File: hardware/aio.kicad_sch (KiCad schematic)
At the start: 39 parts, among them IC1 DAC7562SDGSR, J10 TB007-508-02BE, J11 TB007-508-02BE, J12 TB007-508-02BE, J9 TB007-508-02BE, Q4 MMBT2907ALT1G, Q5 BSP171PH6327XTSA1, U13 TLV9301IDBVR, U14 TLV9301IDBVR, U15 XTR111AIDGQR

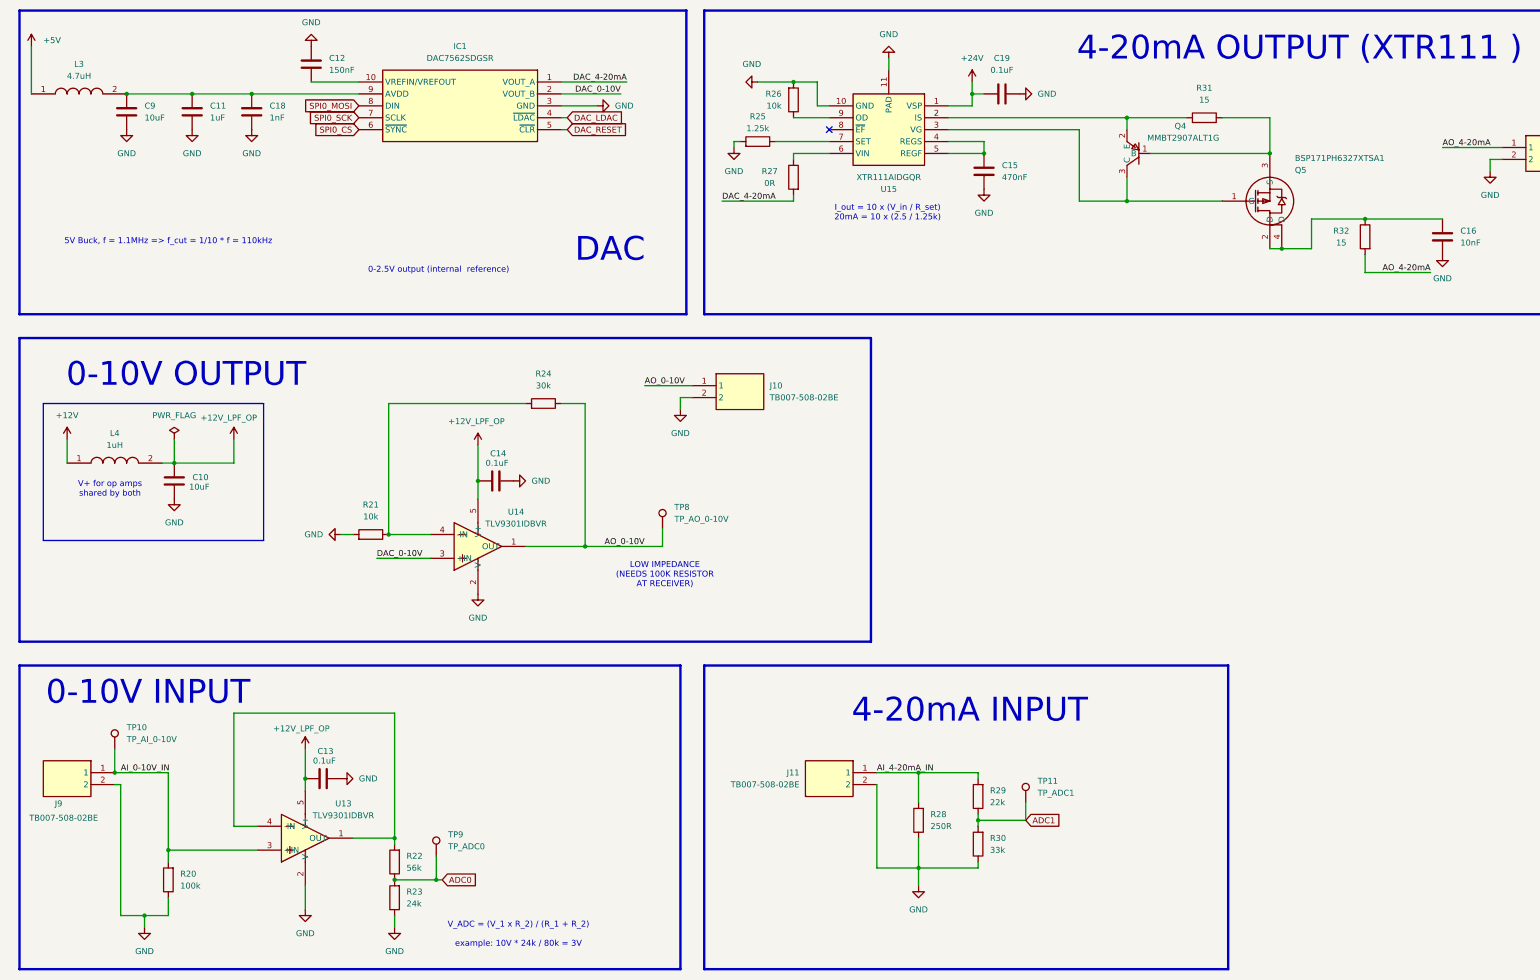
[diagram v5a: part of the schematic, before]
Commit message: Modbus, small schematic changes
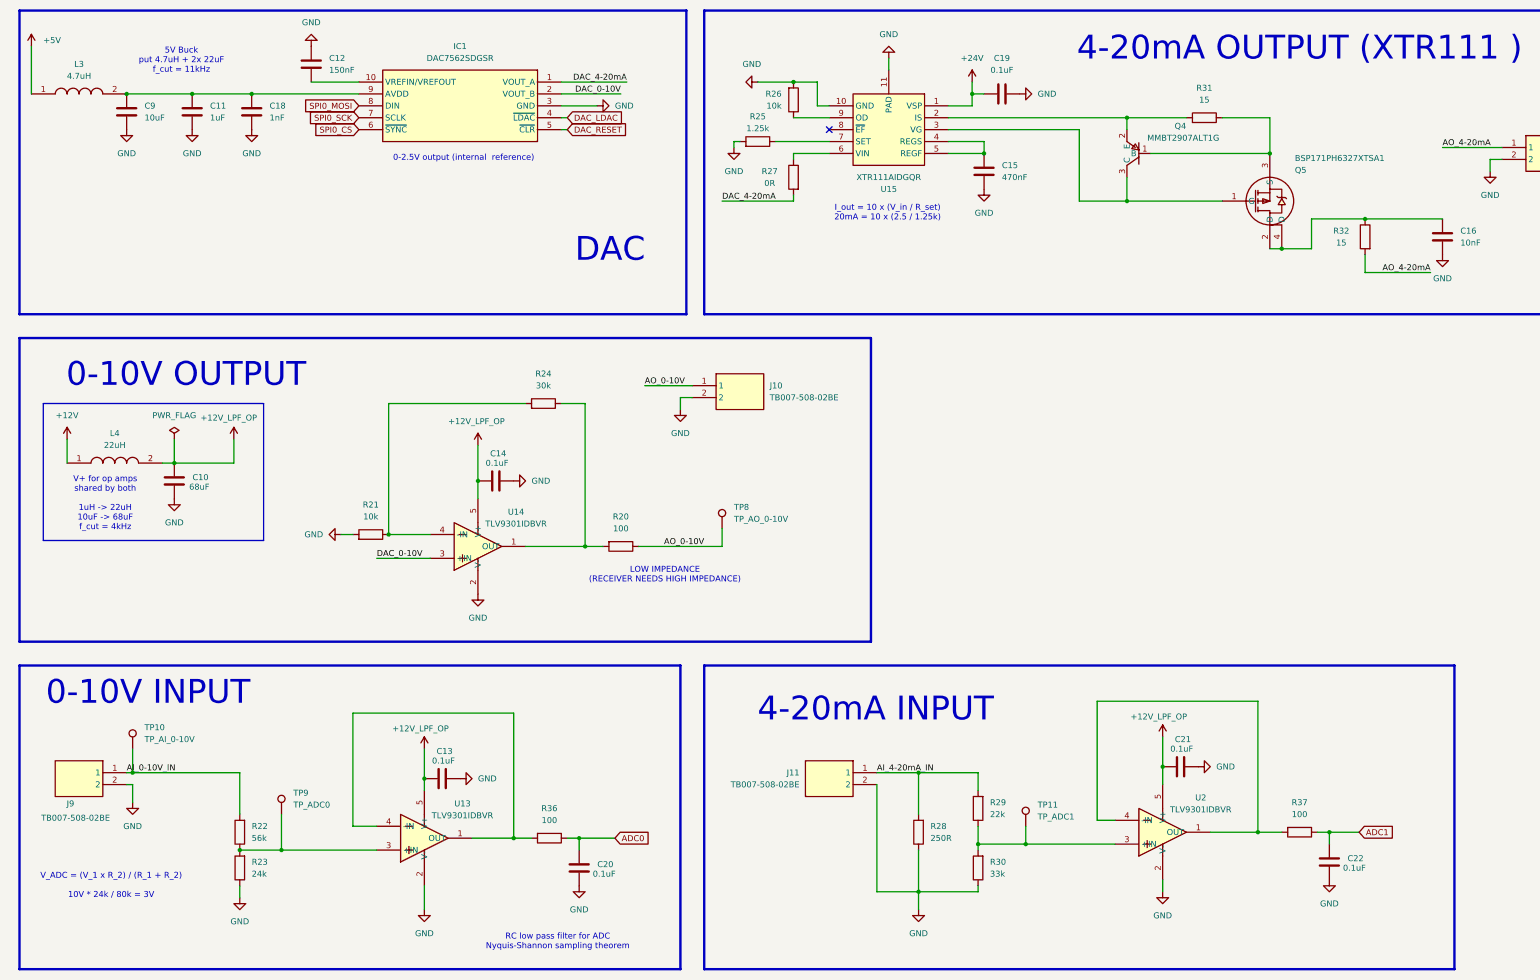
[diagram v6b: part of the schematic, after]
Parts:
- added C20, C21, C22: 0.1uF, Capacitor_SMD:C_1206_3216Metric_Pad1.33x1.80mm_HandSolder, symbol Device:C
- added R36, R37: 100, Resistor_SMD:R_1206_3216Metric_Pad1.30x1.75mm_HandSolder, symbol Device:R
- added U2: TLV9301IDBVR, EasyEDA:SOT-23-5_L3.0-W1.7-P0.95-LS2.8-BR, symbol EasyEDA:TLV9301IDBVR
- C10: value 10uF -> 68uF
- L4: value 1uH -> 22uH
- R20: value 100k -> 100
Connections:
- net +12V_LPF_OP: now also C21.1, U2.5 (V+)
- net ADC0: now also C20.1, R36.1; no longer R22.1, R23.2, TP9.1
- net ADC1: now also C22.1, R37.1; no longer R29.1, R30.2, TP11.1
- net AI_0-10V_IN: now also R22.2; no longer R20.2, U13.3 (+IN)
- net AO_0-10V: now also R20.1; no longer R24.1, U14.1 (OUT)
- net GND: now also C20.2, C21.2, C22.2, U2.2 (V-); no longer R20.1
- net at U13.1 (OUT), U13.4 (-IN): now also R36.2; no longer R22.2
- new net: R20.2, R24.1, U14.1 (OUT)
- new net: R37.2, U2.1 (OUT), U2.4 (-IN)
- new net: R29.1, R30.2, TP11.1, U2.3 (+IN)
- new net: R22.1, R23.2, TP9.1, U13.3 (+IN)
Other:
- note added: "5V Buck put 4.7uH + 2x 22uF f_cut = 11kHz"
- note added: "LOW IMPEDANCE (RECEIVER NEEDS HIGH IMPEDANCE)"
- note added: "RC low pass filter for ADC Nyquis-Shannon sampling theorem"
- note added: "V+ for op amps shared by both 1uH -> 22uH 10uF -> 68uF f_cut = 4kHz"
- note added: "V_ADC = (V_1 x R_2) / (R_1 + R_2) 10V * 24k / 80k = 3V"
- note removed: "5V Buck, f = 1.1MHz => f_cut = 1/10 * f = 110kHz"
- note removed: "LOW IMPEDANCE (NEEDS 100K RESISTOR AT RECEIVER)"
- note removed: "V+ for op amps shared by both"
- note removed: "V_ADC = (V_1 x R_2) / (R_1 + R_2) example: 10V * 24k / 80k = 3V"
- moved on the sheet: C13, J9, R20, R22, R23, R28, R29, R30, TP10, TP11, TP8, TP9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

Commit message: Modbus library done
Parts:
- C10: value 68uF -> 22uF
- C20, C22: value 0.1uF -> 3.3nF
- C9: value 10uF -> 22uF
- L4: value 22uH -> 4.7uH
- R36, R37: value 100 -> 1k
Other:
- note added: "5V Buck put 4.7uH + 2 22uF f_cut = 15kHz"
- note added: "V+ for op amps shared"
- note removed: "5V Buck put 4.7uH + 2x 22uF f_cut = 11kHz"
- note removed: "V+ for op amps shared by both 1uH -> 22uH 10uF -> 68uF f_cut = 4kHz"
- moved on the sheet: C10, C13, C14, C16, C20, C21, C22, J10, J11, J9, L4, Q4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

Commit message: UART parity and better timing handling
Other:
- title: (none) -> Analog IO
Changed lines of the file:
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@@
 	(generator_version "9.0")
 	(paper "A3")
+	(title_block
+		(title "Analog IO")
+	)
 	(rectangle
 		(start 161.29 157.48)
